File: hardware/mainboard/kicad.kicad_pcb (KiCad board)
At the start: 2 copper layers, 100 x 70 mm, 102 parts, among them J1 Screw_Terminal_01x02, J10 Conn_01x10, J2 Screw_Terminal_01x03, J3 Screw_Terminal_01x03, J4 Screw_Terminal_01x03, J5 Conn_01x03, J6 ICSP, J7 Conn_01x05, J8 Conn_01x03, J9 Conn_01x03, K1 RELAY, K2 RELAY, K3 RELAY, Q1 BC817, Q2 BC817, Q3 BC817, Q4 BC817, Q5 IRLML2502, SW1 SW_Push, SW2 SW_Push, U1 DS1233A-10, U10 PC817XI, U11 PC817XI, U12 PC817XI, U2 ESP32, U3 LM2596S-3.3, U4 AMS1117-5.0, U5 ACS759, U6 ACS712, U7 PC817XI, U8 PC817XI, U9 PC817XI

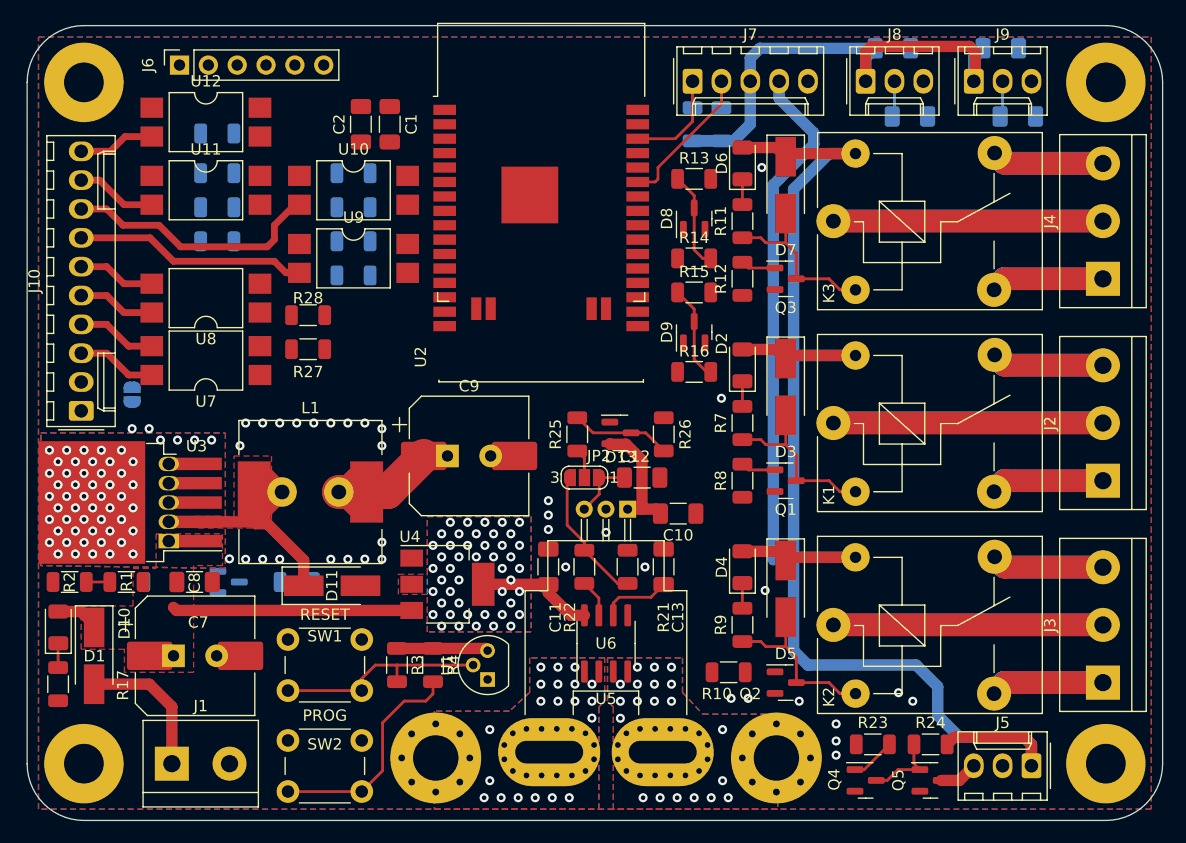
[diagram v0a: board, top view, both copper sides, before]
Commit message: Mainboard routeado.
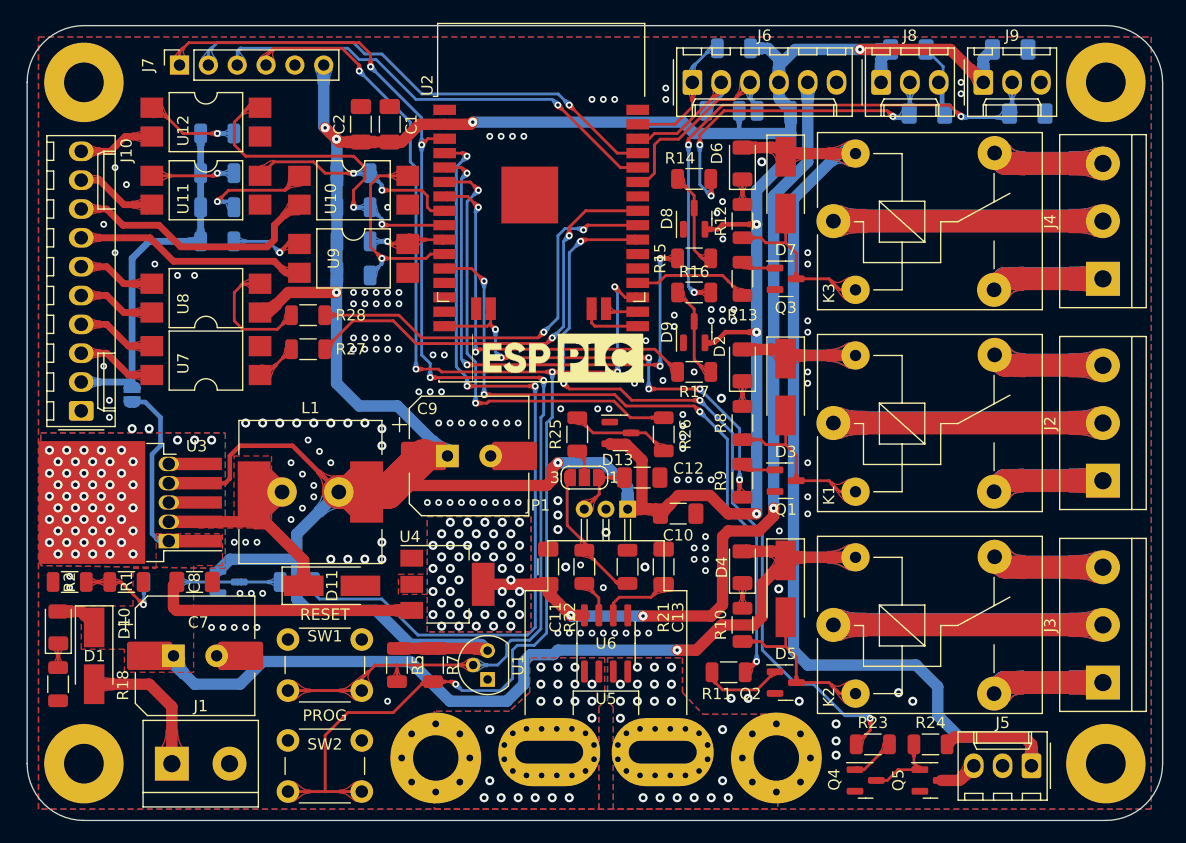
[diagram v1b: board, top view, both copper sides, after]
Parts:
- removed the J7 at (149.9, 55.9)
- removed the R5 at (152.4, 59.7)
- added J6: Conn_01x06, Connector_Molex:Molex_KK-254_AE-6410-06A_1x06_P2.54mm_Vertical, F.Cu at (149.8, 56.0)
- added R3: 10k, Resistor_SMD:R_1206_3216Metric, B.Cu at (157.0, 58.5)
- added R4: 10k, Resistor_SMD:R_1206_3216Metric, B.Cu at (153.5, 53.0)
- moved R6 2.90 mm to (152.5, 58.5), turned to 180 degrees
- moved C3 1.52 mm to (170.5, 58.8)
- moved C6 1.36 mm to (168.9, 53.1)
- moved J8 1.36 mm to (166.5, 56.0)
- moved C5 0.87 mm to (179.3, 58.8)
- moved C4 0.84 mm to (177.8, 53.1)
- moved J9 0.84 mm to (175.5, 56.0)
- renumbered J6 to J7, JP2 to JP1, JP3 to JP2, R9 to R10, R10 to R11, R11 to R12, R12 to R13, R13 to R14, R14 to R15, R15 to R16, R16 to R17, R17 to R18, R3 to R5, R4 to R7, R7 to R8, R8 to R9
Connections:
- U2 pad 26: FAN_1 -> RELAY_3
- U2 pad 29: unconnected-(U2-Pad29) -> FAN_1
- U2 pad 37: RELAY_3 -> INT
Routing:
- net +3V3: track 72.2 -> 293.1 mm, vias 0 -> 9
- net GPIO0: track 19.9 -> 126.6 mm, vias 0 -> 6
- net RESET: track 19.4 -> 111.0 mm, vias 0 -> 4
- net +12V: track 152.1 -> 234.9 mm, vias 0 -> 1
- net VBAT: track 0.00 -> 72.7 mm, vias 0 -> 3
- net FAN_1: track 0.00 -> 69.9 mm, vias 0 -> 4
- net RELAY_2: track 0.00 -> 59.0 mm, vias 0 -> 4
- net TBAT: track 0.00 -> 47.6 mm, vias 0 -> 4
- net /LM35: T2/OUT: track 3.19 -> 48.3 mm, vias 0 -> 3
- net TXD0: track 0.00 -> 43.4 mm, vias 0 -> 1
- net RXD0: track 0.00 -> 41.0 mm, vias 0 -> 1
- net RELAY_1: track 0.00 -> 40.2 mm, vias 0 -> 6
- net IBAT: track 0.00 -> 40.0 mm, vias 0 -> 2
- net OUT1: track 0.00 -> 39.1 mm, vias 0 -> 2
- net OUT0: track 0.00 -> 36.9 mm, vias 0 -> 2
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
